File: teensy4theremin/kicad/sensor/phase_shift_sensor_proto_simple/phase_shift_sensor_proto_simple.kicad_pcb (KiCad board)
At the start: 2 copper layers, 94 x 35.6 mm, 23 parts, among them J1 INDUCTOR_IN, J2 INDUCTOR_OUT, J3 ANTENNA, J4 SENSOR, U1 74HC04, U2 sp721, U3 REG_3V3

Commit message: sensor board
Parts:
- added C10: 10pF, Capacitor_THT:C_Disc_D4.3mm_W1.9mm_P5.00mm, F.Cu at (132.1, 119.4)
- added C8: 10pF, Capacitor_THT:C_Disc_D4.3mm_W1.9mm_P5.00mm, F.Cu at (142.2, 119.4)
- added C9: 10pF, Capacitor_THT:C_Disc_D4.3mm_W1.9mm_P5.00mm, F.Cu at (137.2, 114.3)
- R3, R4: value 1M -> 470K
- moved J3 14.8 mm to (147.3, 109.2), turned to 180 degrees
- moved C1 13.0 mm to (144.8, 96.5), turned to 270 degrees
- moved C7 3.59 mm to (139.7, 101.6)
- moved C2 3.59 mm to (134.6, 96.5)
- moved TP1 2.54 mm to (134.6, 106.7)
- moved TP4 2.54 mm to (114.3, 111.8)
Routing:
- net Net-(C1-Pad1): track 50.8 -> 38.1 mm
- net GND: track 145.2 -> 155.4 mm
- net Net-(C8-Pad1): track 0.00 -> 5.11 mm
- net Net-(C10-Pad2): track 0.00 -> 5.11 mm
- net Net-(C2-Pad2): track 50.8 -> 48.5 mm

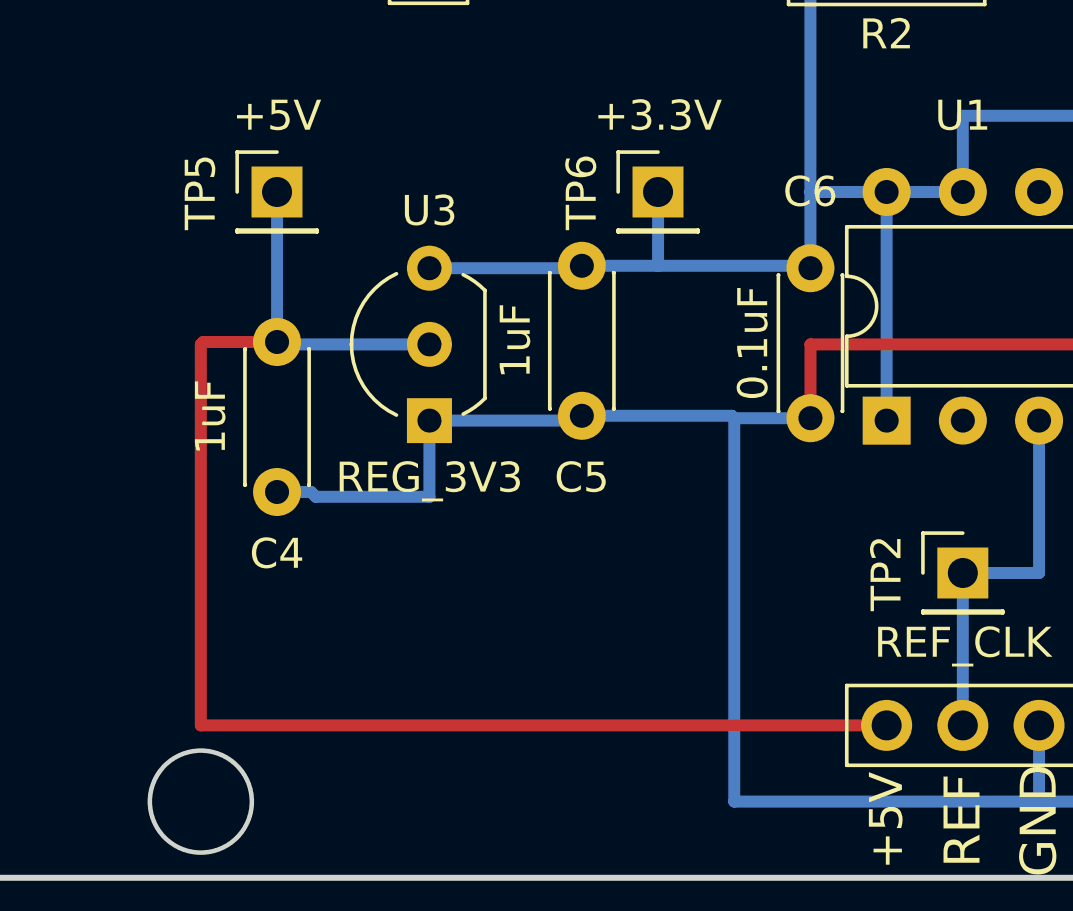
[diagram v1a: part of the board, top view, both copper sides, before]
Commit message: proto pcb - fix 3v3 voltage reg pins
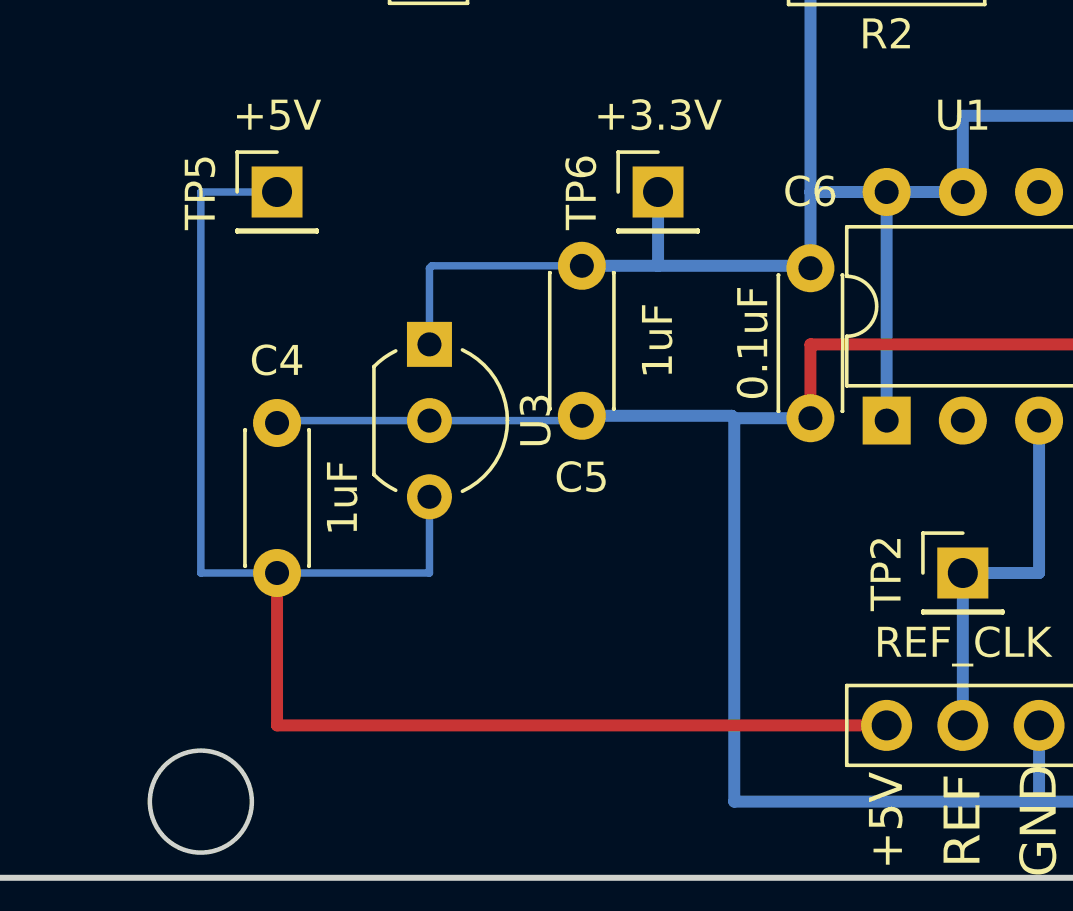
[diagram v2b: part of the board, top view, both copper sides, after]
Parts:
- U3: value REG_3V3 -> L78L33_TO92
- moved C4 7.70 mm to (71.1, 111.8), turned to 90 degrees
- moved U3 2.54 mm to (76.2, 104.1), turned to 270 degrees
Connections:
- U3 pad 1: GND -> +3V3
- U3 pad 2: +5V -> GND
- U3 pad 3: +3V3 -> +5V
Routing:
- net +3V3: track 129.5 -> 132.2 mm
- net GND: track 155.4 -> 152.8 mm
- net +5V: track 48.2 -> 50.8 mm
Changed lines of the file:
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@@
     (add_net "Net-(U2-Pad6)")
+  )
+  (module Package_TO_SOT_THT:TO-92_Inline_Wide (layer F.Cu)
+    (at 76.2 104.14 270)
+    (descr "TO-92 leads in-line, wide, drill 0.75mm (see NXP sot054_po.pdf)")
+    (tags "to-92 sc-43 sc-43a sot54 PA33 transistor")
+    (fp_text reference U3 (at 2.54 -3.56 270) (layer F.SilkS)
+      (effects (font (size 1 1) (thickness 0.15)))
+    )
+    (fp_text value L78L33_TO92 (at 2.54 2.79 270) (layer F.Fab)
+      (effects (font (size 1 1) (thickness 0.15)))
+    )
+    (fp_text user %R (at 2.54 -3.56 270) (layer F.Fab)
+      (effects (font (size 1 1) (thickness 0.15)))
+    )
+    (fp_line (start 0.74 1.85) (end 4.34 1.85) (layer F.SilkS) (width 0.12))
+    (fp_line (start 0.8 1.75) (end 4.3 1.75) (layer F.Fab) (width 0.1))
+    (fp_line (start -1.01 -2.73) (end 6.09 -2.73) (layer F.CrtYd) (width 0.05))
+    (fp_line (start -1.01 -2.73) (end -1.01 2.01) (layer F.CrtYd) (width 0.05))
+    (fp_line (start 6.09 2.01) (end 6.09 -2.73) (layer F.CrtYd) (width 0.05))
+    (fp_line (start 6.09 2.01) (end -1.01 2.01) (layer F.CrtYd) (width 0.05))
+    (fp_arc (start 2.54 0) (end 0.74 1.85) (angle 20) (layer F.SilkS) (width 0.12))
+    (fp_arc (start 2.54 0) (end 2.54 -2.6) (angle -65) (layer F.SilkS) (width 0.12))
+    (fp_arc (start 2.54 0) (end 2.54 -2.6) (angle 65) (layer F.SilkS) (width 0.12))
+    (fp_arc (start 2.54 0) (end 2.54 -2.48) (angle 135) (layer F.Fab) (width 0.1))
+    (fp_arc (start 2.54 0) (end 2.54 -2.48) (angle -135) (layer F.Fab) (width 0.1))
+    (fp_arc (start 2.54 0) (end 4.34 1.85) (angle -20) (layer F.SilkS) (width 0.12))
+    (pad 2 thru_hole circle (at 2.54 0) (size 1.5 1.5) (drill 0.8) (layers *.Cu *.Mask)
+      (net 2 GND))
+    (pad 3 thru_hole circle (at 5.08 0) (size 1.5 1.5) (drill 0.8) (layers *.Cu *.Mask)
+      (net 7 +5V))
+    (pad 1 thru_hole rect (at 0 0) (size 1.5 1.5) (drill 0.8) (layers *.Cu *.Mask)
+      (net 1 +3V3))
+    (model ${KISYS3DMOD}/Package_TO_SOT_THT.3dshapes/TO-92_Inline_Wide.wrl
+      (at (xyz 0 0 0))
+      (scale (xyz 1 1 1))
+      (rotate (xyz 0 0 0))
+    )
   )
   (module Capacitor_THT:C_Disc_D4.3mm_W1.9mm_P5.00mm (layer F.Cu)
@@
       (effects (font (size 1 1) (thickness 0.15)))
     )
-    (fp_text value 1uF (at 2.5 2.2 270) (layer F.SilkS)
+    (fp_text value 1uF (at 2.5 -2.54 270) (layer F.SilkS)
       (effects (font (size 1 1) (thickness 0.15)))
     )
@@
   )
   (module Capacitor_THT:C_Disc_D4.3mm_W1.9mm_P5.00mm (layer F.Cu)
-    (at 71.12 104.06 270)
+    (at 71.12 111.76 90)
     (descr "C, Disc series, Radial, pin pitch=5.00mm, , diameter*width=4.3*1.9mm^2, Capacitor, http://www.vishay.com/docs/45233/krseries.pdf")
     (tags "C Disc series Radial pin pitch 5.00mm  diameter 4.3mm width 1.9mm Capacitor")
-    (fp_text reference C4 (at 7.065 0) (layer F.SilkS)
-      (effects (font (size 1 1) (thickness 0.15)))
-    )
-    (fp_text value 1uF (at 2.5 2.2 270) (layer F.SilkS)
-      (effects (font (size 1 1) (thickness 0.15)))
-    )
-    (fp_text user %R (at 2.5 0 270) (layer F.Fab)
+    (fp_text reference C4 (at 7.065 0 -180) (layer F.SilkS)
+      (effects (font (size 1 1) (thickness 0.15)))
+    )
+    (fp_text value 1uF (at 2.5 2.2 90) (layer F.SilkS)
+      (effects (font (size 1 1) (thickness 0.15)))
+    )
+    (fp_text user %R (at 2.5 0 90) (layer F.Fab)
       (effects (font (size 0.86 0.86) (thickness 0.129)))
     )
@@
     (fp_line (start 0.35 0.95) (end 4.65 0.95) (layer F.Fab) (width 0.1))
     (fp_line (start 0.35 -0.95) (end 0.35 0.95) (layer F.Fab) (width 0.1))
-    (pad 2 thru_hole circle (at 5 0 270) (size 1.6 1.6) (drill 0.8) (layers *.Cu *.Mask)
+    (pad 2 thru_hole circle (at 5 0 90) (size 1.6 1.6) (drill 0.8) (layers *.Cu *.Mask)
       (net 2 GND))
-    (pad 1 thru_hole circle (at 0 0 270) (size 1.6 1.6) (drill 0.8) (layers *.Cu *.Mask)
+    (pad 1 thru_hole circle (at 0 0 90) (size 1.6 1.6) (drill 0.8) (layers *.Cu *.Mask)
       (net 7 +5V))
     (model ${KISYS3DMOD}/Capacitor_THT.3dshapes/C_Disc_D4.3mm_W1.9mm_P5.00mm.wrl
@@
       (net 2 GND))
     (model ${KISYS3DMOD}/Capacitor_THT.3dshapes/C_Disc_D4.3mm_W1.9mm_P5.00mm.wrl
-      (at (xyz 0 0 0))
-      (scale (xyz 1 1 1))
-      (rotate (xyz 0 0 0))
-    )
-  )
-  (module Package_TO_SOT_THT:TO-92_Inline_Wide (layer F.Cu)
-    (at 76.2 106.68 90)
-    (descr "TO-92 leads in-line, wide, drill 0.75mm (see NXP sot054_po.pdf)")
-    (tags "to-92 sc-43 sc-43a sot54 PA33 transistor")
-    (fp_text reference U3 (at 6.985 0 180) (layer F.SilkS)
-      (effects (font (size 1 1) (thickness 0.15)))
-    )
-    (fp_text value REG_3V3 (at -1.905 0 180) (layer F.SilkS)
-      (effects (font (size 1 1) (thickness 0.15)))
-    )
-    (fp_text user %R (at 2.54 -3.56 90) (layer F.Fab)
-      (effects (font (size 1 1) (thickness 0.15)))
-    )
-    (fp_line (start 0.74 1.85) (end 4.34 1.85) (layer F.SilkS) (width 0.12))
-    (fp_line (start 0.8 1.75) (end 4.3 1.75) (layer F.Fab) (width 0.1))
-    (fp_line (start -1.01 -2.73) (end 6.09 -2.73) (layer F.CrtYd) (width 0.05))
-    (fp_line (start -1.01 -2.73) (end -1.01 2.01) (layer F.CrtYd) (width 0.05))
-    (fp_line (start 6.09 2.01) (end 6.09 -2.73) (layer F.CrtYd) (width 0.05))
-    (fp_line (start 6.09 2.01) (end -1.01 2.01) (layer F.CrtYd) (width 0.05))
-    (fp_arc (start 2.54 0) (end 0.74 1.85) (angle 20) (layer F.SilkS) (width 0.12))
-    (fp_arc (start 2.54 0) (end 2.54 -2.6) (angle -65) (layer F.SilkS) (width 0.12))
-    (fp_arc (start 2.54 0) (end 2.54 -2.6) (angle 65) (layer F.SilkS) (width 0.12))
-    (fp_arc (start 2.54 0) (end 2.54 -2.48) (angle 135) (layer F.Fab) (width 0.1))
-    (fp_arc (start 2.54 0) (end 2.54 -2.48) (angle -135) (layer F.Fab) (width 0.1))
-    (fp_arc (start 2.54 0) (end 4.34 1.85) (angle -20) (layer F.SilkS) (width 0.12))
-    (pad 2 thru_hole circle (at 2.54 0 180) (size 1.5 1.5) (drill 0.8) (layers *.Cu *.Mask)
-      (net 7 +5V))
-    (pad 3 thru_hole circle (at 5.08 0 180) (size 1.5 1.5) (drill 0.8) (layers *.Cu *.Mask)
-      (net 1 +3V3))
-    (pad 1 thru_hole rect (at 0 0 180) (size 1.5 1.5) (drill 0.8) (layers *.Cu *.Mask)
-      (net 2 GND))
-    (model ${KISYS3DMOD}/Package_TO_SOT_THT.3dshapes/TO-92_Inline_Wide.wrl
       (at (xyz 0 0 0))
       (scale (xyz 1 1 1))
@@
   )
   (segment (start 81.2 101.6) (end 81.28 101.52) (width 0.4) (layer B.Cu) (net 1))
-  (segment (start 76.2 101.6) (end 81.2 101.6) (width 0.4) (layer B.Cu) (net 1))
   (segment (start 88.9 101.6) (end 88.9 99.06) (width 0.4) (layer B.Cu) (net 1))
   (segment (start 91.44 99.06) (end 93.98 99.06) (width 0.4) (layer B.Cu) (net 1))
@@
   (segment (start 83.82 101.52) (end 88.82 101.52) (width 0.4) (layer B.Cu) (net 1))
   (segment (start 114.3 101.6) (end 116.84 101.6) (width 0.4) (layer B.Cu) (net 1))
+  (segment (start 76.2 104.14) (end 76.2 101.6) (width 0.25) (layer B.Cu) (net 1))
+  (segment (start 76.28 101.52) (end 81.28 101.52) (width 0.25) (layer B.Cu) (net 1))
+  (segment (start 76.2 101.6) (end 76.28 101.52) (width 0.25) (layer B.Cu) (net 1))
   (segment (start 81.12 106.36) (end 81.28 106.52) (width 0.4) (layer B.Cu) (net 2))
-  (segment (start 81.12 106.68) (end 81.28 106.52) (width 0.4) (layer B.Cu) (net 2))
-  (segment (start 76.2 106.68) (end 81.12 106.68) (width 0.4) (layer B.Cu) (net 2))
   (segment (start 86.28 106.52) (end 86.36 106.6) (width 0.4) (layer B.Cu) (net 2))
   (segment (start 81.28 106.52) (end 86.28 106.52) (width 0.4) (layer B.Cu) (net 2))
-  (segment (start 72.25137 109.06) (end 72.41137 109.22) (width 0.4) (layer B.Cu) (net 2))
-  (segment (start 71.12 109.06) (end 72.25137 109.06) (width 0.4) (layer B.Cu) (net 2))
-  (segment (start 72.41137 109.22) (end 76.2 109.22) (width 0.4) (layer B.Cu) (net 2))
-  (segment (start 76.2 109.22) (end 76.2 106.68) (width 0.4) (layer B.Cu) (net 2))
   (segment (start 124.46 106.68) (end 124.46 109.22) (width 0.4) (layer B.Cu) (net 2))
   (segment (start 124.46 109.22) (end 119.38 109.22) (width 0.4) (layer B.Cu) (net 2))
@@
   (segment (start 93.98 111.76) (end 96.52 111.76) (width 0.4) (layer B.Cu) (net 5))
   (segment (start 96.52 111.76) (end 96.52 106.68) (width 0.4) (layer B.Cu) (net 5))
-  (segment (start 71.2 104.14) (end 71.12 104.06) (width 0.4) (layer B.Cu) (net 7))
-  (segment (start 76.2 104.14) (end 71.2 104.14) (width 0.4) (layer B.Cu) (net 7))
-  (segment (start 71.12 104.06) (end 71.12 99.06) (width 0.4) (layer B.Cu) (net 7))
-  (segment (start 68.58 116.84) (end 91.44 116.84) (width 0.4) (layer F.Cu) (net 7))
-  (segment (start 68.58 104.14) (end 68.58 116.84) (width 0.4) (layer F.Cu) (net 7))
-  (segment (start 71.12 104.06) (end 68.66 104.06) (width 0.4) (layer F.Cu) (net 7))
-  (segment (start 68.66 104.06) (end 68.58 104.14) (width 0.4) (layer F.Cu) (net 7))
+  (segment (start 81.12 106.68) (end 81.28 106.52) (width 0.25) (layer B.Cu) (net 2))
+  (segment (start 76.2 106.68) (end 81.12 106.68) (width 0.25) (layer B.Cu) (net 2))
+  (segment (start 71.2 106.68) (end 71.12 106.76) (width 0.25) (layer B.Cu) (net 2))
+  (segment (start 76.2 106.68) (end 71.2 106.68) (width 0.25) (layer B.Cu) (net 2))
+  (segment (start 76.2 111.76) (end 76.2 109.22) (width 0.25) (layer B.Cu) (net 7))
+  (segment (start 71.12 111.76) (end 76.2 111.76) (width 0.25) (layer B.Cu) (net 7))
+  (segment (start 71.12 111.76) (end 68.58 111.76) (width 0.25) (layer B.Cu) (net 7))
+  (segment (start 68.58 111.76) (end 68.58 99.06) (width 0.25) (layer B.Cu) (net 7))
+  (segment (start 68.58 99.06) (end 71.12 99.06) (width 0.25) (layer B.Cu) (net 7))
+  (segment (start 71.12 116.84) (end 91.44 116.84) (width 0.4) (layer F.Cu) (net 7))
+  (segment (start 71.12 111.76) (end 71.12 116.84) (width 0.4) (layer F.Cu) (net 7))
   (segment (start 142.24 114.38) (end 147.24 114.38) (width 0.25) (layer B.Cu) (net 13))
   (segment (start 147.32 114.3) (end 147.32 109.22) (width 0.25) (layer B.Cu) (net 13))
